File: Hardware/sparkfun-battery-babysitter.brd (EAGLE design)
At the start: 33 x 33 mm, 56 parts, among them U1 BQ24075, U2 BQ27441-G1

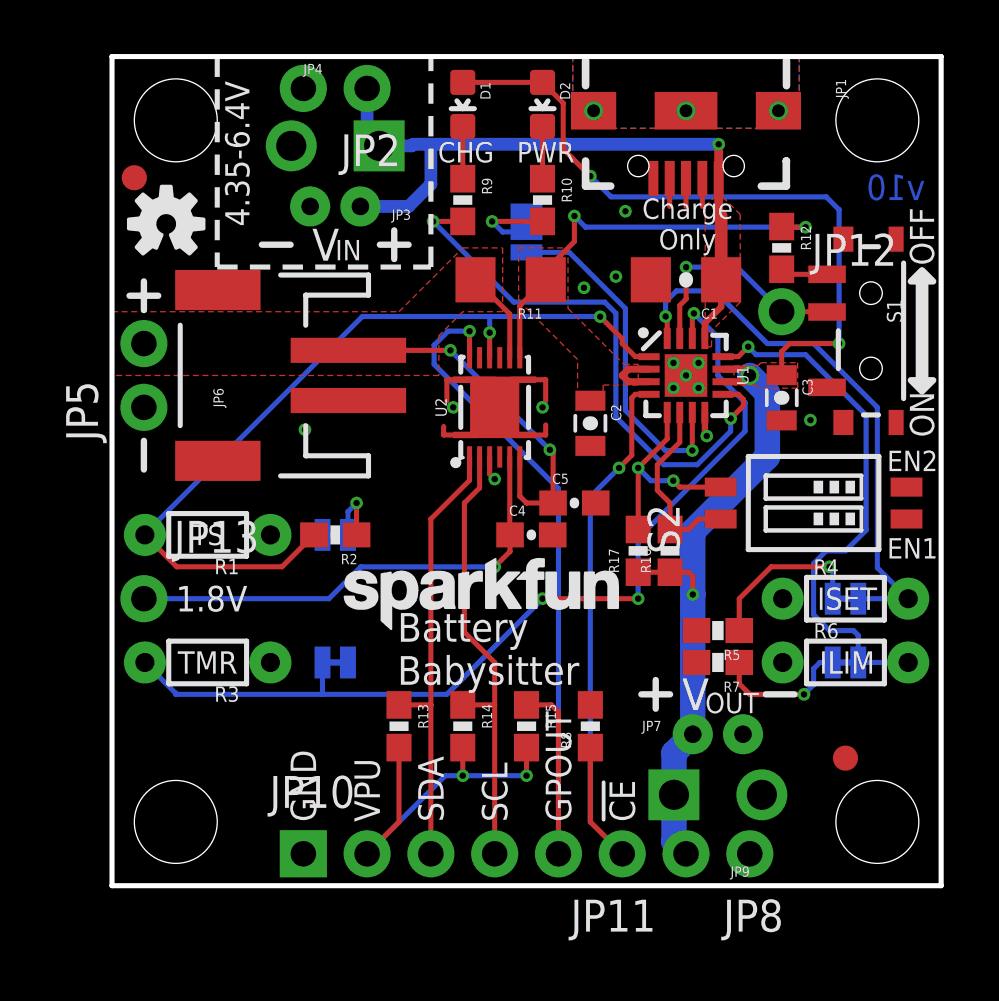
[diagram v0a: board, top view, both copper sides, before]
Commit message: Break out D+/D-, silkscreen fixes
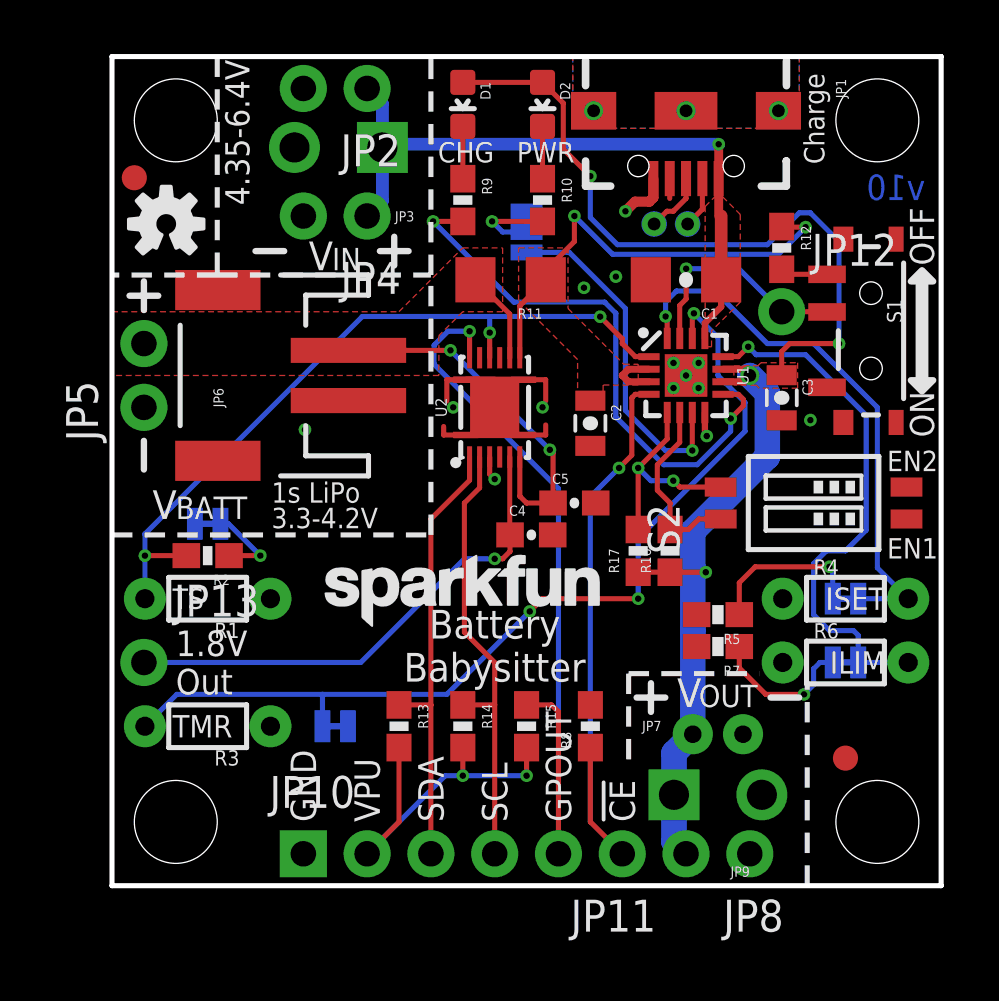
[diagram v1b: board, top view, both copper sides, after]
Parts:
- added TP1, TP2: (no value), SparkFun-Passives:PAD.03X.04
- JP4: device SparkFun-Connectors:JST-2-PTH-NS -> SparkFun-Connectors:1X02_NO_SILK
- moved R2 5.15 mm to (3.81, 13.1)
- moved SJ1 5.10 mm to (3.81, 14.4)
- moved R1 2.54 mm to (3.81, 11.4)
- moved R3 2.54 mm to (3.81, 6.35)
- moved SJ2 2.54 mm to (8.89, 6.35)
- moved JP13 2.54 mm to (1.27, 8.89)
- moved JP4 1.33 mm to (10.2, 26.7), turned to 180 degrees
- moved LOGO2 1.09 mm to (22.4, 18.3)
- moved LOGO1 0.77 mm to (8.00, 9.84)
- moved R5 0.63 mm to (24.1, 10.8)
- moved R7 0.63 mm to (24.1, 9.53)
- moved JP3 0.14 mm to (10.8, 29.4)
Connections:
- net D+: now also TP2.P$1
- net D-: now also TP1.P$1
- net GND: now also JP4.2; no longer JP4.1
- net V_USB: now also JP4.1; no longer JP4.2
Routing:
- net TS: track 33.9 -> 30.3 mm, vias 2 -> 3
- net GND: track 8.68 -> 10.8 mm
- net V_USB: track 28.8 -> 27.0 mm
- net OUT: track 55.0 -> 56.5 mm
- net D+: track 1.11 -> 2.48 mm, vias 0 -> 1
- net 1.8V: track 19.1 -> 20.2 mm
- net D-: track 1.11 -> 2.05 mm, vias 0 -> 1
- net V_BATT: track 19.2 -> 20.1 mm
- net N$1: track 2.68 -> 3.36 mm
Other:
- board text added: "1.8V (Out)"
- board text added: "1.8V Out"
- board text added: "1s LiPo"
- board text added: "3.3-4.2V"
- board text added: "BATT"
- board text added: "Charge"
- board text added: "D+"
- board text added: "D-"
- board text removed: "1.8V"
- board text removed: "Charge Only"

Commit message: Small silk fixes after run through checklist
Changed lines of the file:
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@@
 <setting verticaltext="up"/>
 </settings>
-<grid distance="0.025" unitdist="inch" unit="inch" style="lines" multiple="1" display="yes" altdistance="0.0025" altunitdist="inch" altunit="inch"/>
+<grid distance="0.05" unitdist="inch" unit="inch" style="lines" multiple="1" display="yes" altdistance="0.005" altunitdist="inch" altunit="inch"/>
 <layers>
 <layer number="1" name="Top" color="4" fill="1" visible="yes" active="yes"/>
@@
 <text x="24.0665" y="14.1605" size="0.8128" layer="22" font="vector" ratio="15" rot="MR0" align="bottom-center">2</text>
 <text x="22.7965" y="14.1605" size="0.8128" layer="22" font="vector" ratio="15" rot="MR0" align="bottom-center">1</text>
-<text x="32.385" y="27.305" size="1.016" layer="16" ratio="15" rot="MR0">v10</text>
+<text x="0.381" y="25.781" size="1.016" layer="16" ratio="15" rot="MR90">v10</text>
 <text x="2.159" y="8.89" size="1.016" layer="22" font="vector" ratio="15" rot="MR0" align="center-right">1.8V
 (Out)</text>
@@
 <contactref element="JP1" pad="D+1"/>
 <contactref element="TP2" pad="P$1"/>
-<via x="21.59" y="26.3525" extent="1-16" drill="0.508" diameter="0.9652"/>
+<via x="21.59" y="26.3525" extent="1-16" drill="0.508" diameter="0.9652" alwaysstop="yes"/>
 <wire x1="22.86" y1="28.161" x2="22.86" y2="27.3685" width="0.2032" layer="1"/>
 <wire x1="22.86" y1="27.3685" x2="22.352" y2="26.8605" width="0.2032" layer="1"/>
@@
 <wire x1="23.51" y1="28.161" x2="23.51" y2="26.939" width="0.2032" layer="1"/>
 <contactref element="TP1" pad="P$1"/>
-<via x="22.9235" y="26.3525" extent="1-16" drill="0.508" diameter="0.9652"/>
+<via x="22.9235" y="26.3525" extent="1-16" drill="0.508" diameter="0.9652" alwaysstop="yes"/>
 <wire x1="23.51" y1="26.939" x2="22.9235" y2="26.3525" width="0.2032" layer="1"/>
 </signal>

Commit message: Reverting version to v02 - proto round 2
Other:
- board text added: "v02"
- board text removed: "v10"
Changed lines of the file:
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@@
 <layer number="47" name="Measures" color="7" fill="1" visible="no" active="yes"/>
 <layer number="48" name="Document" color="7" fill="1" visible="no" active="yes"/>
-<layer number="49" name="Reference" color="7" fill="1" visible="yes" active="yes"/>
+<layer number="49" name="Reference" color="7" fill="1" visible="no" active="yes"/>
 <layer number="50" name="dxf" color="7" fill="1" visible="no" active="no"/>
 <layer number="51" name="tDocu" color="6" fill="1" visible="yes" active="yes"/>
@@
 <text x="24.0665" y="14.1605" size="0.8128" layer="22" font="vector" ratio="15" rot="MR0" align="bottom-center">2</text>
 <text x="22.7965" y="14.1605" size="0.8128" layer="22" font="vector" ratio="15" rot="MR0" align="bottom-center">1</text>
-<text x="0.381" y="25.781" size="1.016" layer="16" ratio="15" rot="MR90">v10</text>
+<text x="0.381" y="25.781" size="1.016" layer="16" ratio="15" rot="MR90">v02</text>
 <text x="2.159" y="8.89" size="1.016" layer="22" font="vector" ratio="15" rot="MR0" align="center-right">1.8V
 (Out)</text>

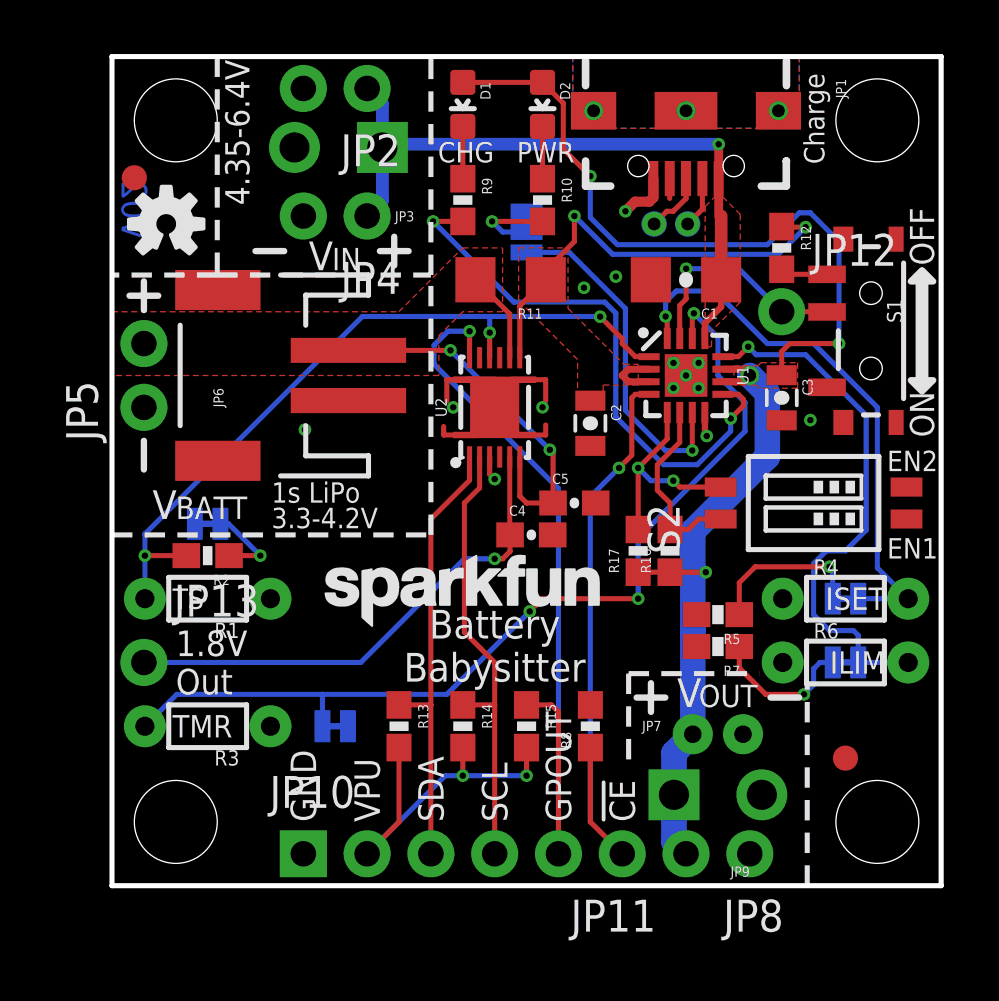
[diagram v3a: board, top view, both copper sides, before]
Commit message: Moving some silk, nudging a via, upping to v10
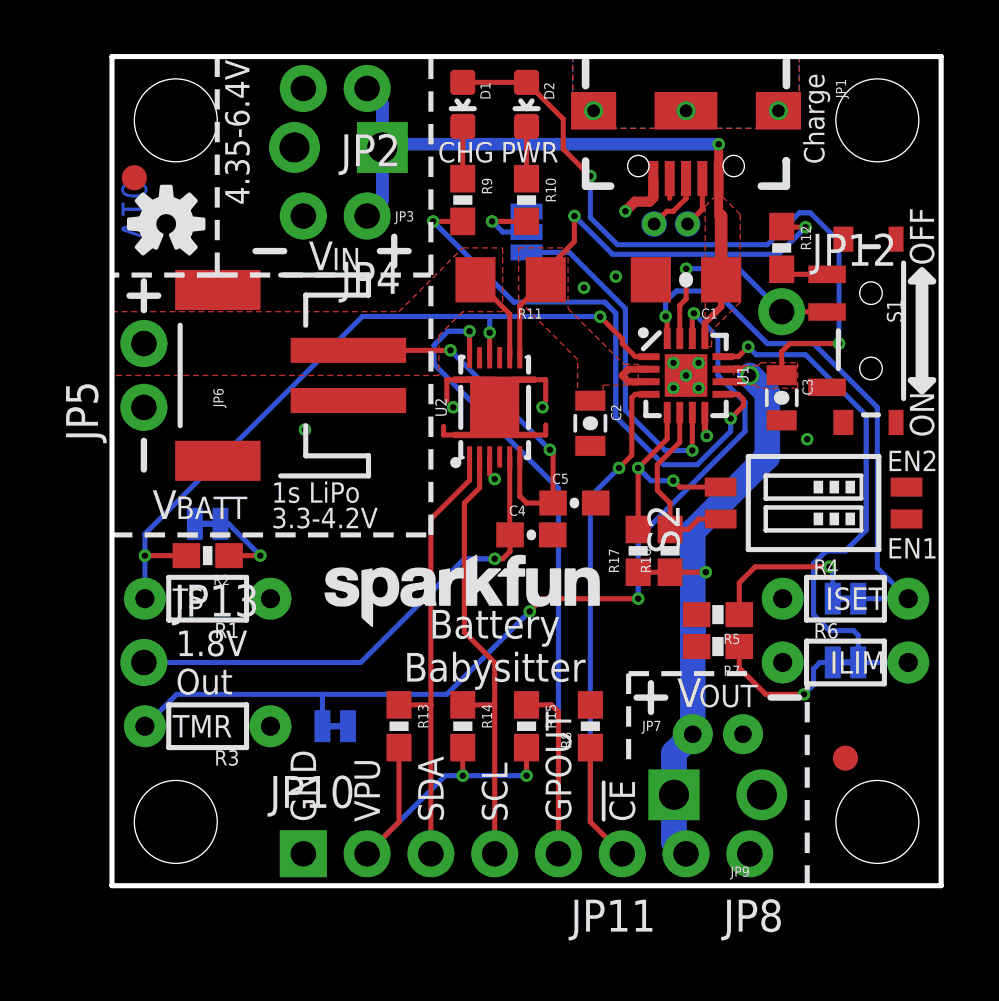
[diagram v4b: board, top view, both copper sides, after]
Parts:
- moved LOGO2 2.52 mm to (22.9, 15.8)
- moved D2 0.63 mm to (16.5, 31.1)
- moved R10 0.63 mm to (16.5, 27.3)
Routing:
- net N$5: track 3.55 -> 2.92 mm
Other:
- board text added: "100mA"
- board text added: "500mA"
- board text added: "I"
- board text added: "v10"
- board text removed: "100"
- board text removed: "500"
- board text removed: "CUR"
- board text removed: "v02"
